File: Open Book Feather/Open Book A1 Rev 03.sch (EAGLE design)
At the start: 124 parts, among them J1 SJ-43514-SMT, J2 10118193-0001LF, Q1 DMG341, Q2 IRLML0100, SW1 SPDT_SWITCH, U1 AP2112-3.3, U2 MCP73831T-2ACI/OT, U3 ATSAMD51J64-TQFP(10X10), U4 GD25Q16C (or GD25Q32C), U5 MCP23008/SO, U6 GD25Q16C (or GD25Q32C), U8 MAX4466EXK+T, X1 JSTPH, X2 2x5 0.05" SWD

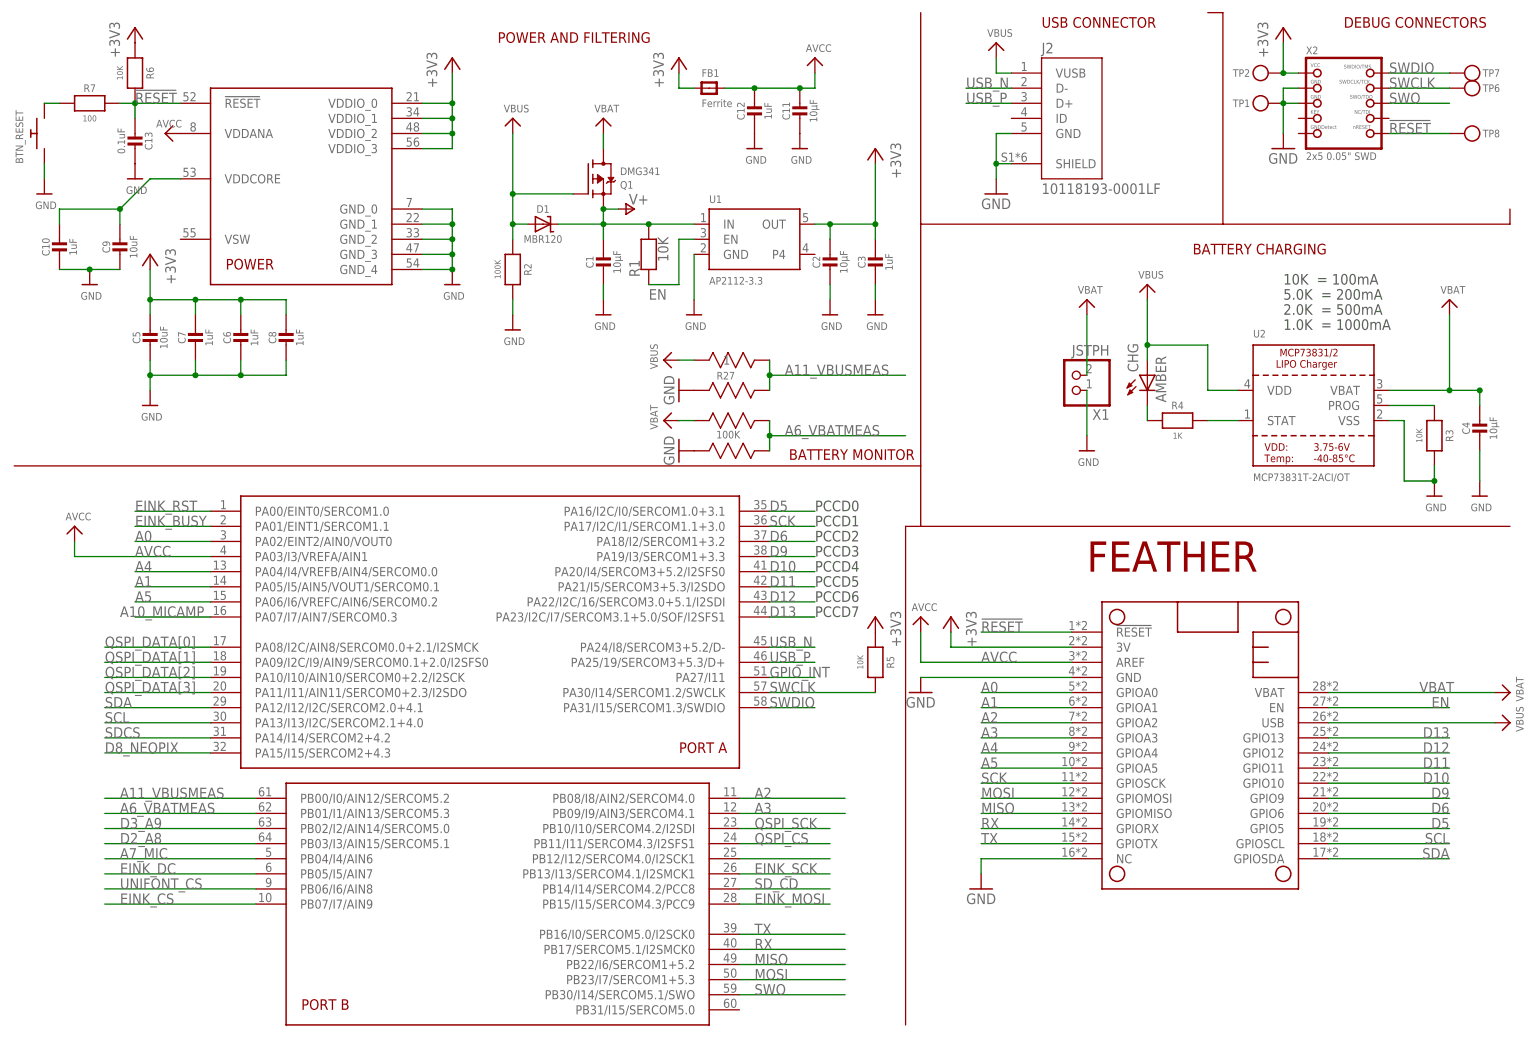
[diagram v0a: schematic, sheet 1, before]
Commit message: add indicator LED for full charge
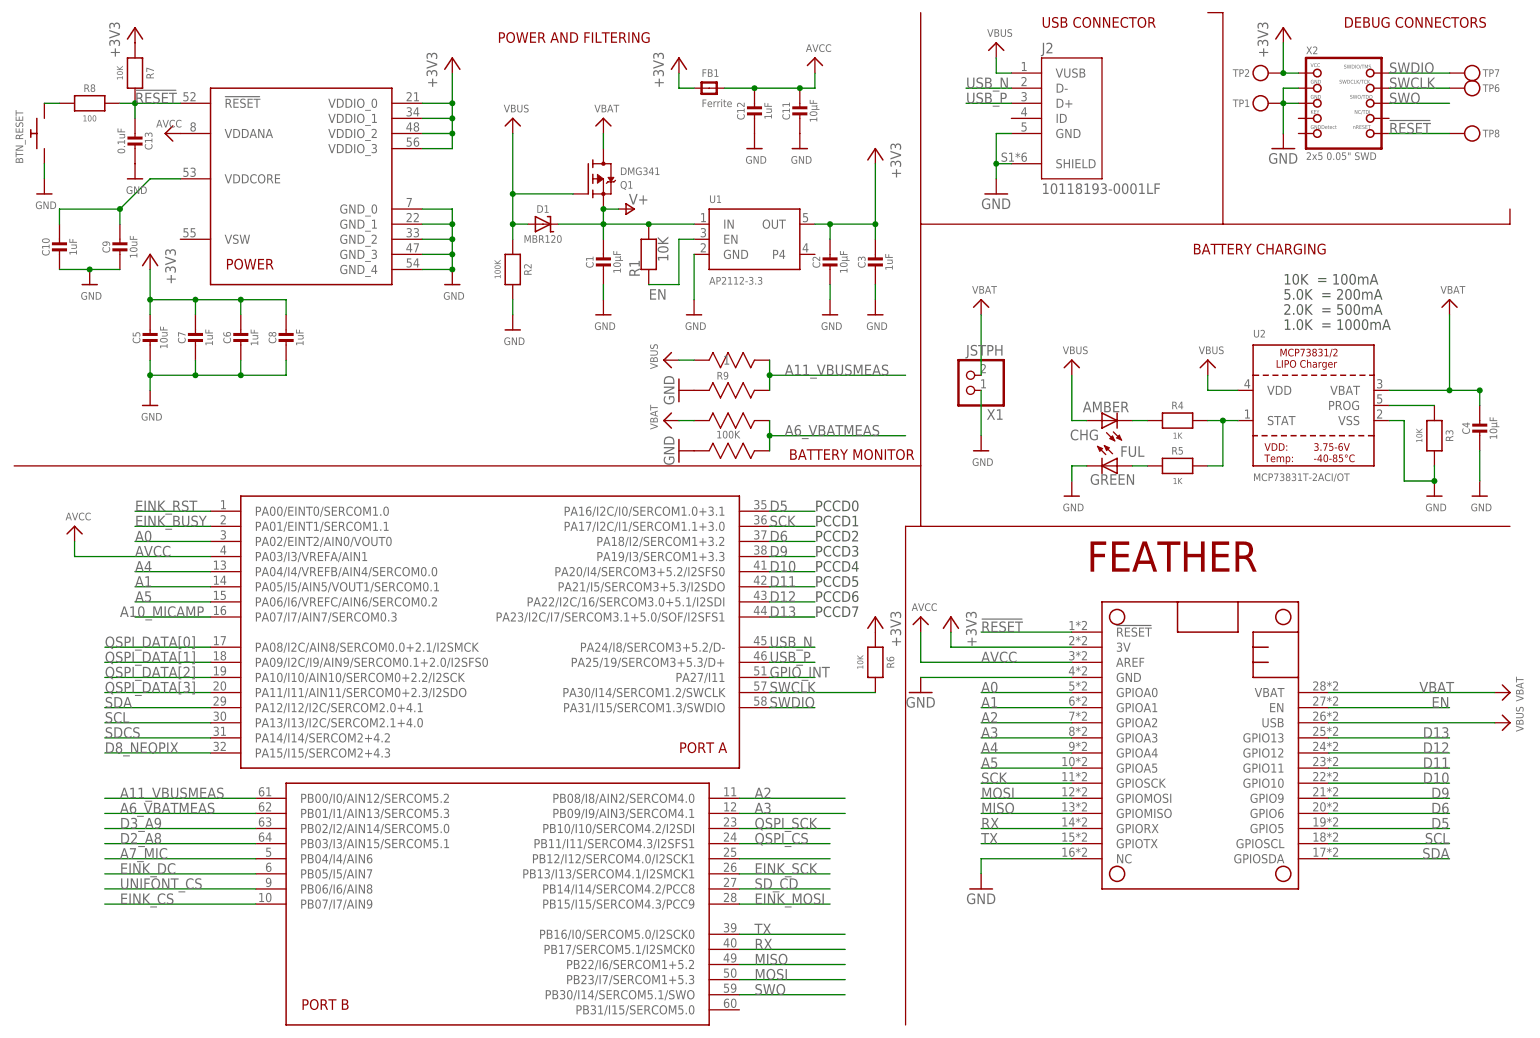
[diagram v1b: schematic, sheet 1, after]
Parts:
- added FUL: GREEN, adafruit:LEDCHIP-LED0805
- added R8: 100, microbuilder:RESISTOR0805_10MGAP
- R5: value 10K -> 1K; device microbuilder:RESISTOR0805_10MGAP -> microbuilder:RESISTOR0805_NOOUTLINE
- R7: value 100 -> 10K
- renumbered R27 to R9
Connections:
- removed net N$5: R4.2, U2.STAT
- new net N$6: FUL.A, R5.1
- new net STAT: R4.2, R5.2, U2.STAT
- net !RESET: now also R8.2; no longer R6.2
- net +3V3: now also R7.1; no longer R5.1
- net GND: now also FUL.C
- net N$1: now also R8.1; no longer R7.1
- net SWCLK: now also R6.2; no longer R5.2
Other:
- moved on the sheet: CHG, R5, R6, R7, X1
